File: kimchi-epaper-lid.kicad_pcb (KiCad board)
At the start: 4 copper layers, 65 x 32 mm, 28 parts, among them J1 DF40HC(3.5)-60DS, J2 DF40HC(3.5)-60DS, Q1 SI1308EDL-T1-BE3, U1 24C32, X1 52435-2471

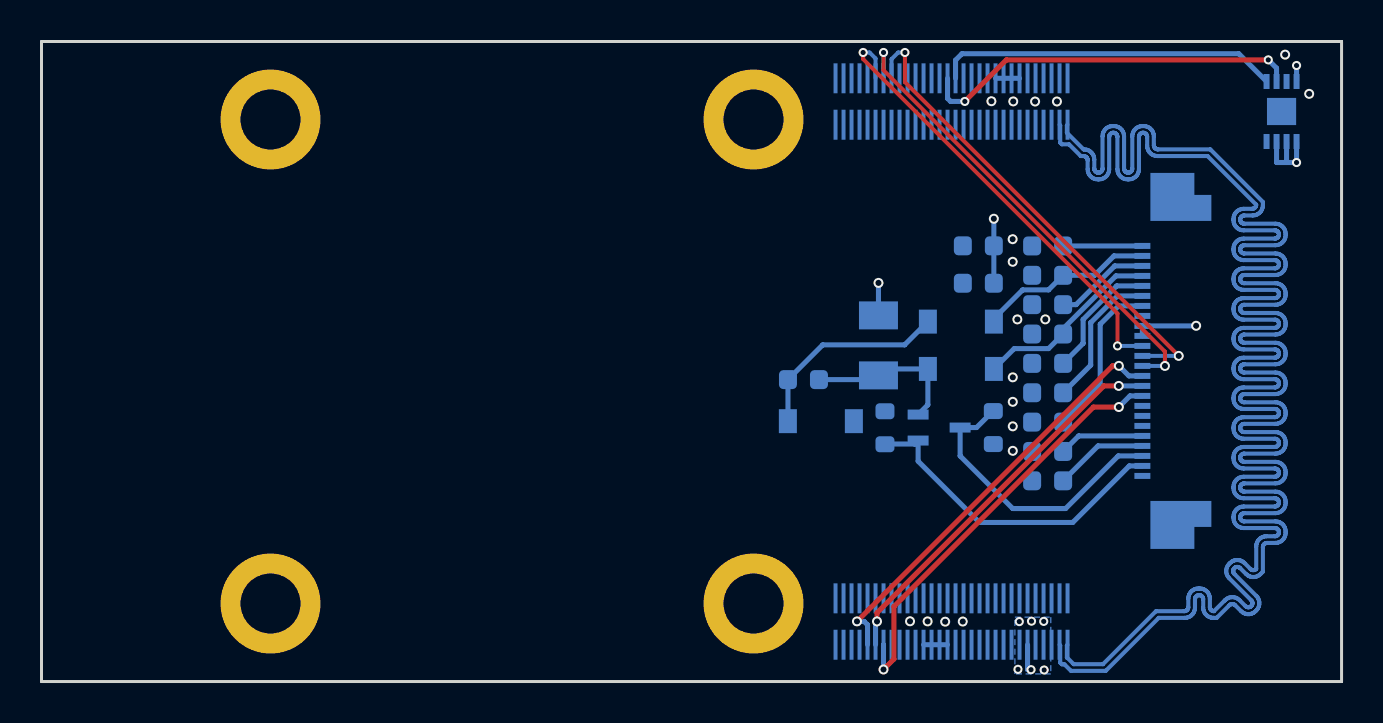
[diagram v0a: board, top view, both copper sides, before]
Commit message: Replaced inductor and completed routing (acq review)
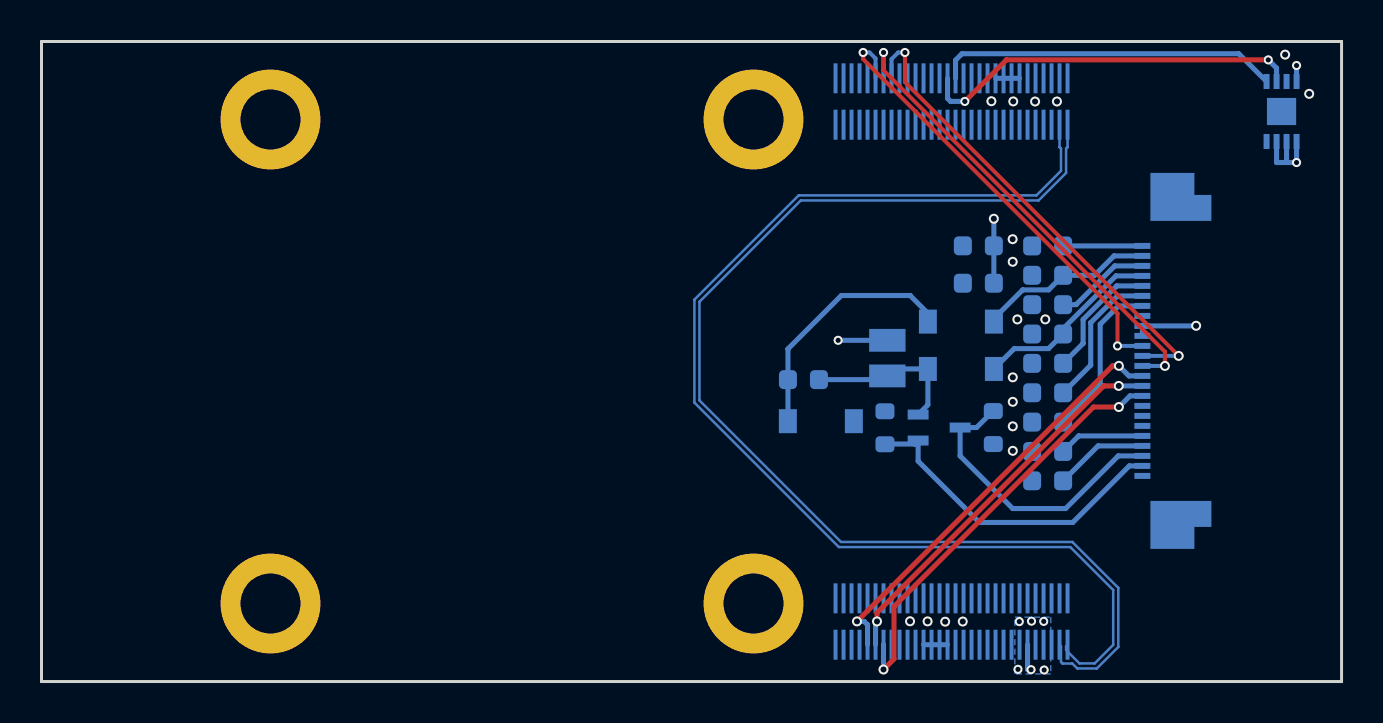
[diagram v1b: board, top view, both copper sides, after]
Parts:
- L1: value 68uH -> LBM2016T680J; footprint NLV32T-680J-EF:INDM3225X240N -> LBM2016T680J:INDC2016X180N
- moved L1 0.78 mm to (149.3, 109.8)
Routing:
- net PCIE_USB_D_N: track 98.5 -> 59.4 mm
- net PCIE_USB_D_P: track 99.4 -> 60.5 mm
- net Net-(C2-Pad1): track 10.3 -> 12.5 mm
- net VDD_3V3: track 14.2 -> 15.1 mm

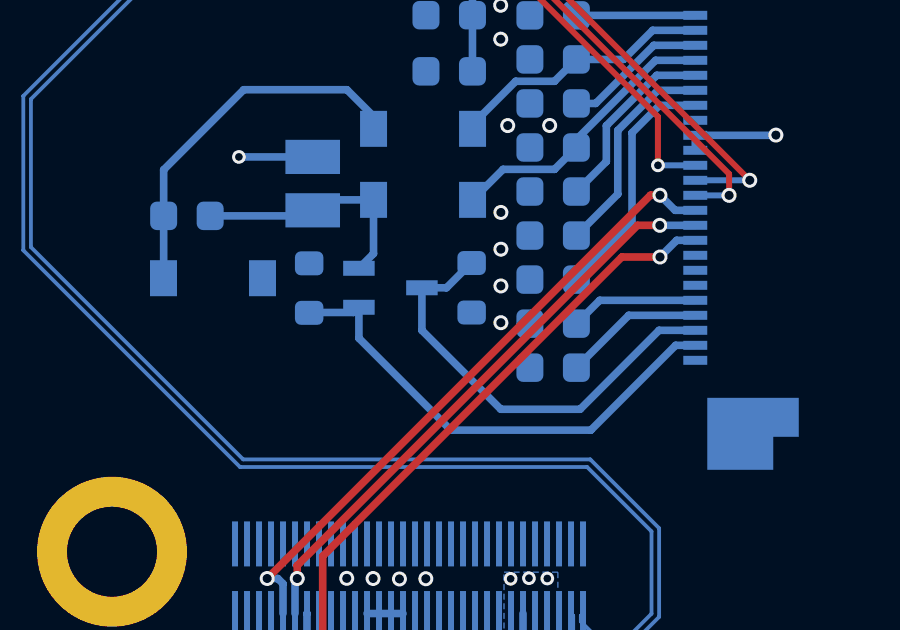
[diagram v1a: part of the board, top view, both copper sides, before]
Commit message: Fixed mistake in mosfet schematics
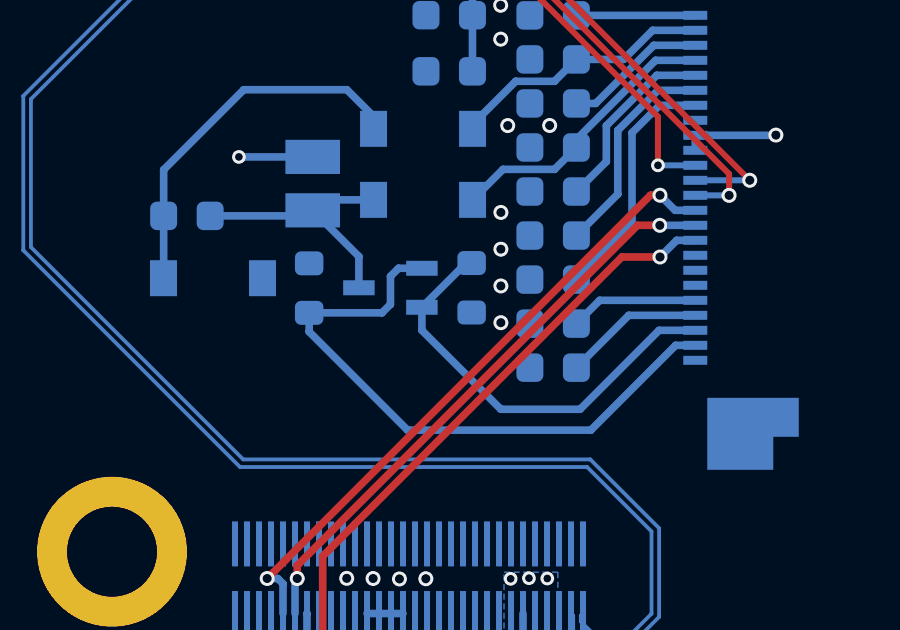
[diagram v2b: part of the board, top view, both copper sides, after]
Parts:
- turned Q1 to 180 degrees
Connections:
- Q1 pad 2: Net-(C2-Pad2) -> RESE
- Q1 pad 3: RESE -> Net-(C2-Pad2)
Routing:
- net GDR: track 16.4 -> 20.9 mm
- net Net-(C2-Pad2): track 8.15 -> 8.89 mm
